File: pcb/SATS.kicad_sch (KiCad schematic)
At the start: 17 parts, among them J1 Raspberry_Pi_2_3, J2 A00-432-262-450, J3 AudioJack4_SwitchTR1, J4 1862042, J5 1862042, SW1 Main Door Switch, SW2 Serv Door Switch, SW3 Third Reed Switch, U1 MCP23017_SP, U2 MCP23017_SP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

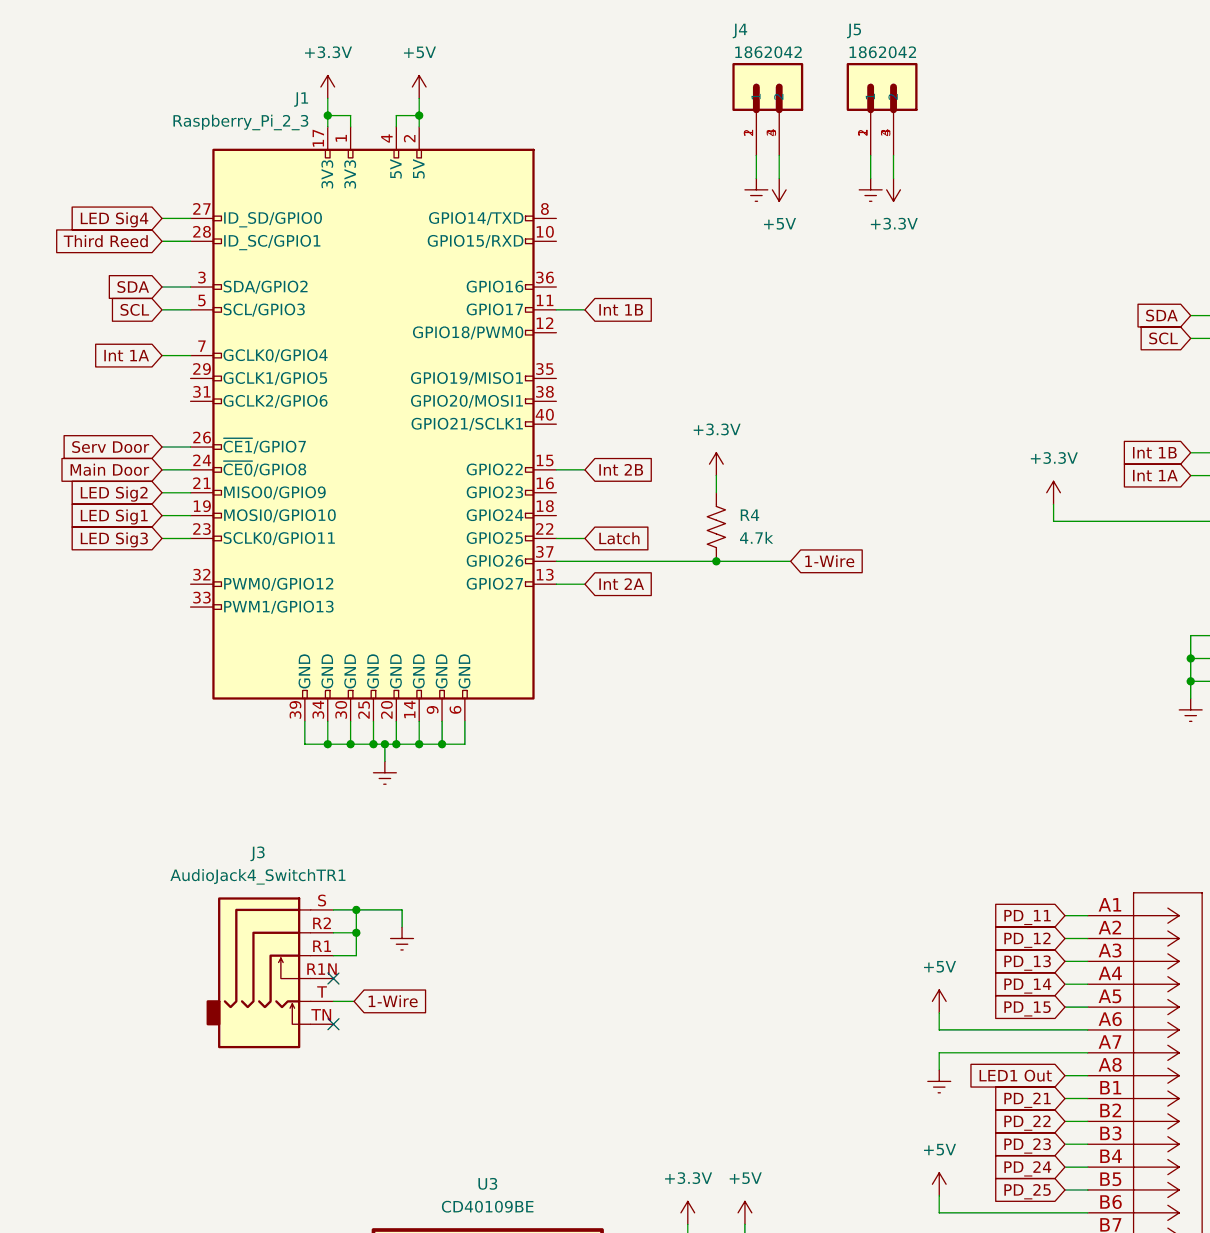
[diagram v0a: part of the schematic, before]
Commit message: Add Card LED Terminals
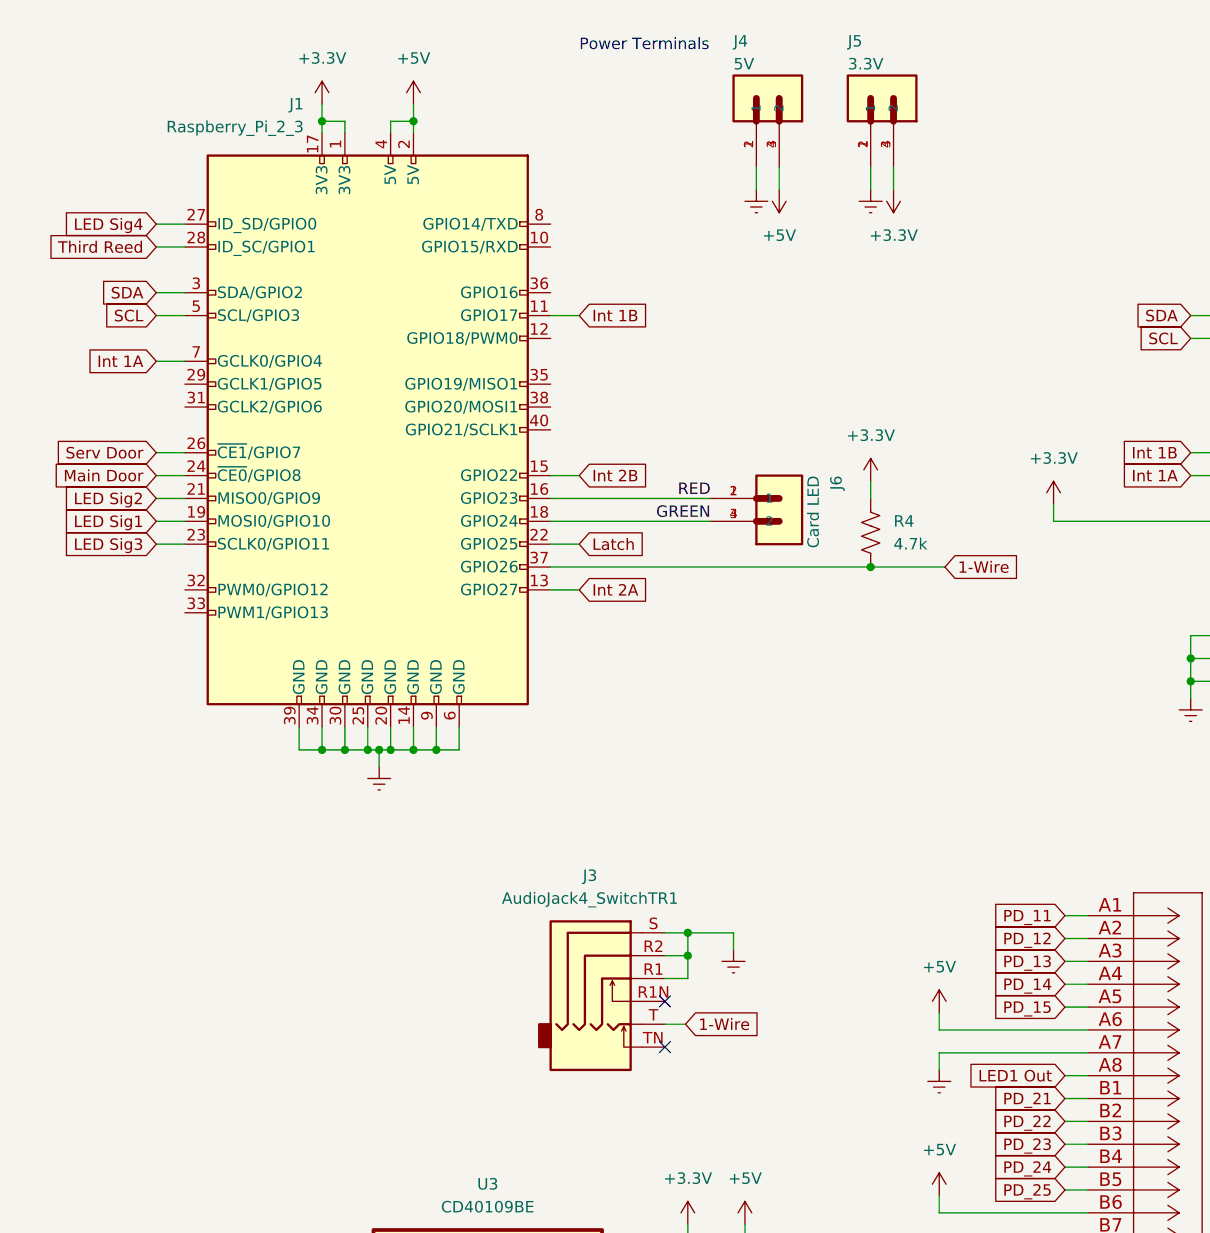
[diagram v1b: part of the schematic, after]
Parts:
- added J6: Card LED, PHOENIX_1862042, symbol TerminalConn:1862042
- J4: value 1862042 -> 5V
- J5: value 1862042 -> 3.3V
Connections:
- net RED: now reaches J1.16 (GPIO23)
- net RED: now also J6.1, J6.2 (1)
- net GREEN: now reaches J1.18 (GPIO24)
- net GREEN: now also J6.3 (2), J6.4 (2)
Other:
- note added: "Power Terminals"
- moved on the sheet: J1, J3, J4, J5, R4

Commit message: Finish Schematic
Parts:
- added C3, C4: 100nF, Capacitor_THT:C_Rect_L7.0mm_W3.5mm_P5.00mm, symbol Device:C
- added J10, J11, J12, J13: EXT_GPIO, TerminalConn:PHOENIX_1862042, symbol TerminalConn:1862042
- added J7: Wiegand, TerminalConn:PHOENIX_1862042, symbol TerminalConn:1862042
- added J8: Beep, TerminalConn:PHOENIX_1862042, symbol TerminalConn:1862042
- added J9: Card Power, TerminalConn:PHOENIX_1862042, symbol TerminalConn:1862042
- J4, J5, J6: footprint PHOENIX_1862042 -> TerminalConn:PHOENIX_1862042
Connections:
- net +3V3: now also C4.1
- net +5V: now also J4.1, J4.2 (1), C3.1, J9.1, J9.2 (1); no longer J4.3 (2), J4.4 (2)
- net Earth: now also J4.3 (2), J4.4 (2), C3.2, C4.2, J8.3 (2), J8.4 (2), J9.3 (2), J9.4 (2); no longer J4.1, J4.2 (1)
- net LED Sig1: now also U3.10 (C); no longer U3.3 (A)
- net LED Sig3: now also U3.14 (D); no longer U3.10 (C)
- net LED Sig4: now also U3.3 (A); no longer U3.14 (D)
- net LED1 Out: now also U3.11 (G); no longer U3.4 (E)
- net LED3 Out: now also U3.13 (H); no longer U3.11 (G)
- net LED4 Out: now also U3.4 (E); no longer U3.13 (H)
- net Wiegand 0: now reaches J1.10 (GPIO15/RXD)
- net Wiegand 0: now also J7.1, J7.2 (1)
- net Wiegand 1: now reaches J1.12 (GPIO18/PWM0)
- net Wiegand 1: now also J7.3 (2), J7.4 (2)
- net EXT_GPIO5: now reaches J1.29 (GCLK1/GPIO5)
- net EXT_GPIO5: now also J10.1, J10.2 (1)
- net EXT_GPIO6: now reaches J1.31 (GCLK2/GPIO6)
- net EXT_GPIO6: now also J10.3 (2), J10.4 (2)
- net EXT_GPIO12: now reaches J1.32 (PWM0/GPIO12)
- net EXT_GPIO12: now also J12.3 (2), J12.4 (2)
- net EXT_GPIO13: now reaches J1.33 (PWM1/GPIO13)
- net EXT_GPIO13: now also J11.1, J11.2 (1)
- net EXT_GPIO19: now reaches J1.35 (GPIO19/MISO1)
- net EXT_GPIO19: now also J11.3 (2), J11.4 (2)
- net EXT_GPIO16: now reaches J1.36 (GPIO16)
- net EXT_GPIO16: now also J12.1, J12.2 (1)
- net EXT_GPIO20: now reaches J1.38 (GPIO20/MOSI1)
- net EXT_GPIO20: now also J13.3 (2), J13.4 (2)
- net EXT_GPIO21: now reaches J1.40 (GPIO21/SCLK1)
- net EXT_GPIO21: now also J13.1, J13.2 (1)
- net Card Beeper: now reaches J1.8 (GPIO14/TXD)
- net Card Beeper: now also J8.1, J8.2 (1)
- net GREEN renamed Card RED
- net Card RED: now also J1.16 (GPIO23); no longer J1.18 (GPIO24)
- net RED renamed Card GRN
- net Card GRN: now also J1.18 (GPIO24); no longer J1.16 (GPIO23)
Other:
- moved on the sheet: C1, C2, D1, J1, J2, J3, J4, J5, J6, L1, R4, SW1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

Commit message: neatify and reorganize
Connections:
- net LED1 Out: now also J2.B8; no longer J2.A8
- net LED2 Out: now also J2.A8; no longer J2.B8
- net PD_11: now also J2.B1; no longer J2.A1
- net PD_12: now also J2.B2; no longer J2.A2
- net PD_13: now also J2.B3; no longer J2.A3
- net PD_14: now also J2.B4; no longer J2.A4
- net PD_15: now also J2.B5; no longer J2.A5
- net PD_21: now also J2.A1; no longer J2.B1
- net PD_22: now also J2.A2; no longer J2.B2
- net PD_23: now also J2.A3; no longer J2.B3
- net PD_24: now also J2.A4; no longer J2.B4
- net PD_25: now also J2.A5; no longer J2.B5
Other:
- moved on the sheet: C1, C2, D1, L1, R4, SW1, SW2, SW3, U1, U2, U4

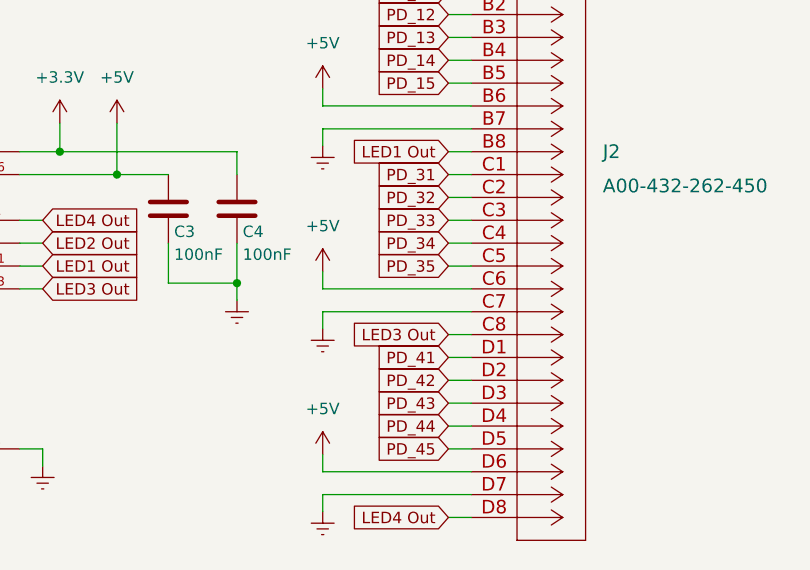
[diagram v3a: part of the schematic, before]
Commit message: Route PD lines
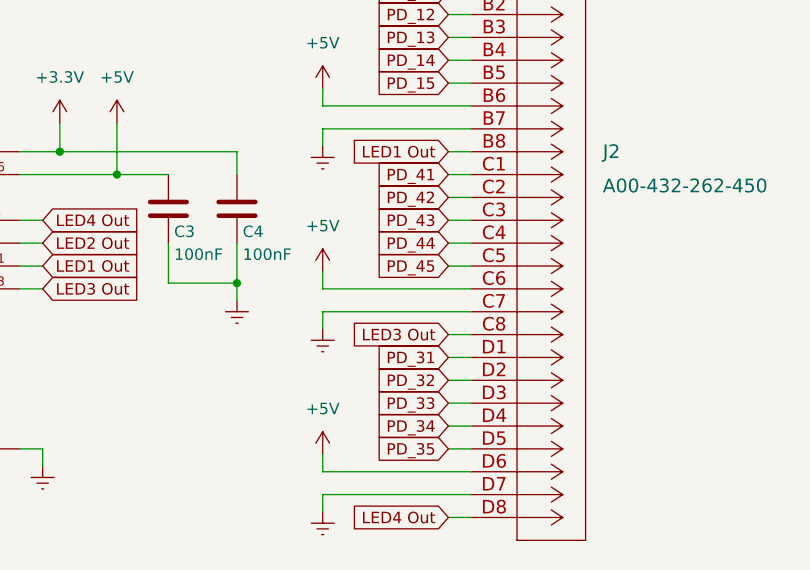
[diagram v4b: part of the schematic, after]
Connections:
- net PD_31: now also J2.D1; no longer J2.C1
- net PD_32: now also J2.D2; no longer J2.C2
- net PD_33: now also J2.D3; no longer J2.C3
- net PD_34: now also J2.D4; no longer J2.C4
- net PD_35: now also J2.D5; no longer J2.C5
- net PD_41: now also J2.C1; no longer J2.D1
- net PD_42: now also J2.C2; no longer J2.D2
- net PD_43: now also J2.C3; no longer J2.D3
- net PD_44: now also J2.C4; no longer J2.D4
- net PD_45: now also J2.C5; no longer J2.D5

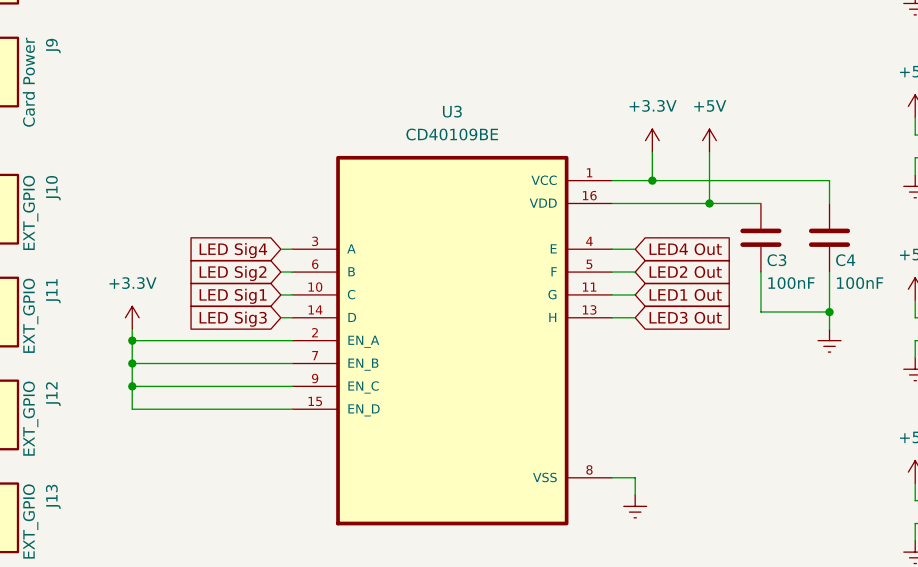
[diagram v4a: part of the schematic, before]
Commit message: Clead PD Lines and route LED Outs
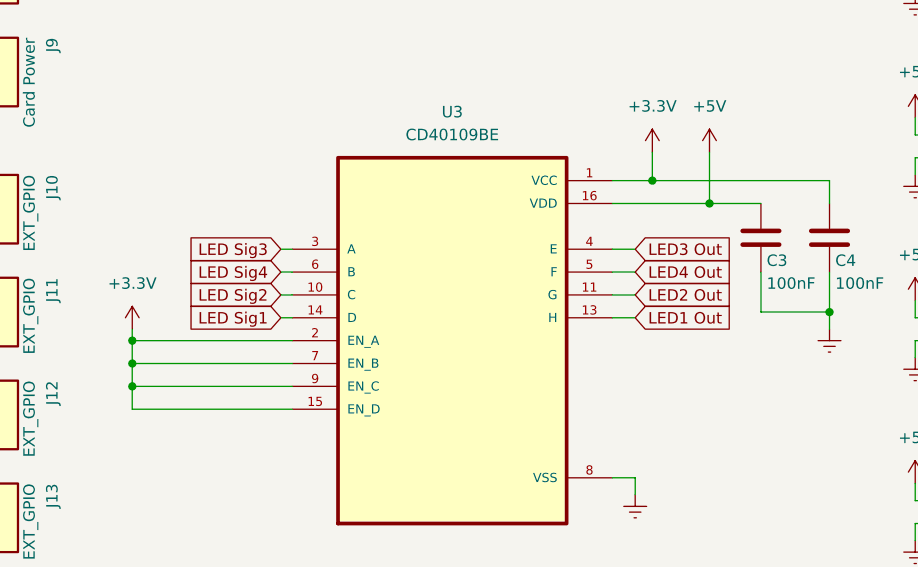
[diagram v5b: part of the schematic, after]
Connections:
- net LED Sig1: now also U3.14 (D); no longer U3.10 (C)
- net LED Sig2: now also U3.10 (C); no longer U3.6 (B)
- net LED Sig3: now also U3.3 (A); no longer U3.14 (D)
- net LED Sig4: now also U3.6 (B); no longer U3.3 (A)
- net LED1 Out: now also U3.13 (H); no longer U3.11 (G)
- net LED2 Out: now also U3.11 (G); no longer U3.5 (F)
- net LED3 Out: now also U3.4 (E); no longer U3.13 (H)
- net LED4 Out: now also U3.5 (F); no longer U3.4 (E)

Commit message: mostly done
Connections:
- net +5V: now also J9.3 (2), J9.4 (2); no longer J9.1, J9.2 (1)
- net EXT_GPIO12: now also J11.1, J11.2 (1); no longer J12.3 (2), J12.4 (2)
- net EXT_GPIO13: now also J11.3 (2), J11.4 (2); no longer J11.1, J11.2 (1)
- net EXT_GPIO19: now also J12.3 (2), J12.4 (2); no longer J11.3 (2), J11.4 (2)
- net Earth: now also J9.1, J9.2 (1); no longer J9.3 (2), J9.4 (2)
- net LED Sig1: now also J1.23 (SCLK0/GPIO11); no longer J1.19 (MOSI0/GPIO10)
- net LED Sig2: now also J1.19 (MOSI0/GPIO10); no longer J1.21 (MISO0/GPIO9)
- net LED Sig3: now also J1.27 (ID_SD/GPIO0); no longer J1.23 (SCLK0/GPIO11)
- net LED Sig4: now also J1.21 (MISO0/GPIO9); no longer J1.27 (ID_SD/GPIO0)
- net Wiegand 0: now also J7.3 (2), J7.4 (2); no longer J7.1, J7.2 (1)
- net Wiegand 1: now also J7.1, J7.2 (1); no longer J7.3 (2), J7.4 (2)
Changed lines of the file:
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@@
     (stroke (width 0) (type default) (color 0 0 0 0))
   )
-  (wire (pts (xy 20.32 138.43) (xy 34.29 138.43))
+  (wire (pts (xy 20.32 140.97) (xy 34.29 140.97))
     (stroke (width 0) (type default) (color 0 0 0 0))
   )
@@
     (stroke (width 0) (type default) (color 0 0 0 0))
   )
-  (wire (pts (xy 31.75 140.97) (xy 31.75 143.51))
+  (wire (pts (xy 31.75 138.43) (xy 31.75 143.51))
     (stroke (width 0) (type default) (color 0 0 0 0))
   )
@@
     (stroke (width 0) (type default) (color 0 0 0 0))
   )
-  (wire (pts (xy 31.75 140.97) (xy 34.29 140.97))
+  (wire (pts (xy 31.75 138.43) (xy 34.29 138.43))
     (stroke (width 0) (type default) (color 0 0 0 0))
   )
@@
     (stroke (width 0) (type default) (color 0 0 0 0))
   )
-  (wire (pts (xy 20.32 135.89) (xy 20.32 138.43))
+  (wire (pts (xy 20.32 138.43) (xy 20.32 140.97))
     (stroke (width 0) (type default) (color 0 0 0 0))
   )
@@
     )
   )
-  (global_label "LED Sig3" (shape input) (at 29.21 70.485 180) (fields_autoplaced)
+  (global_label "LED Sig3" (shape input) (at 29.21 34.925 180) (fields_autoplaced)
+    (effects (font (size 1.27 1.27)) (justify right))
+    (property "Intersheet References" "${INTERSHEET_REFS}" (id 0) (at 18.2093 35.0044 0)
+      (effects (font (size 1.27 1.27)) (justify right) hide)
+    )
+  )
+  (global_label "LED Sig1" (shape input) (at 29.21 70.485 180) (fields_autoplaced)
     (effects (font (size 1.27 1.27)) (justify right))
     (property "Intersheet References" "${INTERSHEET_REFS}" (id 0) (at 18.2093 70.4056 0)
@@
     )
   )
-  (global_label "LED Sig1" (shape input) (at 29.21 67.945 180) (fields_autoplaced)
-    (effects (font (size 1.27 1.27)) (justify right))
-    (property "Intersheet References" "${INTERSHEET_REFS}" (id 0) (at 18.2093 67.8656 0)
-      (effects (font (size 1.27 1.27)) (justify right) hide)
-    )
-  )
-  (global_label "Wiegand 0" (shape input) (at 30.48 115.57 180) (fields_autoplaced)
-    (effects (font (size 1.27 1.27)) (justify right))
-    (property "Intersheet References" "${INTERSHEET_REFS}" (id 0) (at 18.1488 115.4906 0)
+  (global_label "Wiegand 0" (shape input) (at 30.48 118.11 180) (fields_autoplaced)
+    (effects (font (size 1.27 1.27)) (justify right))
+    (property "Intersheet References" "${INTERSHEET_REFS}" (id 0) (at 18.1488 118.1894 0)
       (effects (font (size 1.27 1.27)) (justify right) hide)
     )
@@
     )
   )
-  (global_label "EXT_GPIO12" (shape input) (at 30.48 179.07 180) (fields_autoplaced)
-    (effects (font (size 1.27 1.27)) (justify right))
-    (property "Intersheet References" "${INTERSHEET_REFS}" (id 0) (at 16.8788 178.9906 0)
+  (global_label "EXT_GPIO12" (shape input) (at 30.48 165.1 180) (fields_autoplaced)
+    (effects (font (size 1.27 1.27)) (justify right))
+    (property "Intersheet References" "${INTERSHEET_REFS}" (id 0) (at 16.8788 165.0206 0)
       (effects (font (size 1.27 1.27)) (justify right) hide)
     )
@@
     )
   )
-  (global_label "EXT_GPIO13" (shape input) (at 30.48 165.1 180) (fields_autoplaced)
-    (effects (font (size 1.27 1.27)) (justify right))
-    (property "Intersheet References" "${INTERSHEET_REFS}" (id 0) (at 16.8788 165.0206 0)
+  (global_label "EXT_GPIO13" (shape input) (at 30.48 167.64 180) (fields_autoplaced)
+    (effects (font (size 1.27 1.27)) (justify right))
+    (property "Intersheet References" "${INTERSHEET_REFS}" (id 0) (at 16.8788 167.7194 0)
       (effects (font (size 1.27 1.27)) (justify right) hide)
     )
@@
     )
   )
-  (global_label "EXT_GPIO19" (shape input) (at 30.48 167.64 180) (fields_autoplaced)
-    (effects (font (size 1.27 1.27)) (justify right))
-    (property "Intersheet References" "${INTERSHEET_REFS}" (id 0) (at 16.8788 167.5606 0)
+  (global_label "EXT_GPIO19" (shape input) (at 30.48 179.07 180) (fields_autoplaced)
+    (effects (font (size 1.27 1.27)) (justify right))
+    (property "Intersheet References" "${INTERSHEET_REFS}" (id 0) (at 16.8788 179.1494 0)
       (effects (font (size 1.27 1.27)) (justify right) hide)
     )
@@
     )
   )
-  (global_label "Wiegand 1" (shape input) (at 30.48 118.11 180) (fields_autoplaced)
-    (effects (font (size 1.27 1.27)) (justify right))
-    (property "Intersheet References" "${INTERSHEET_REFS}" (id 0) (at 18.1488 118.0306 0)
+  (global_label "Wiegand 1" (shape input) (at 30.48 115.57 180) (fields_autoplaced)
+    (effects (font (size 1.27 1.27)) (justify right))
+    (property "Intersheet References" "${INTERSHEET_REFS}" (id 0) (at 18.1488 115.6494 0)
       (effects (font (size 1.27 1.27)) (justify right) hide)
     )
@@
     )
   )
-  (global_label "LED Sig4" (shape input) (at 29.21 34.925 180) (fields_autoplaced)
-    (effects (font (size 1.27 1.27)) (justify right))
-    (property "Intersheet References" "${INTERSHEET_REFS}" (id 0) (at 18.2093 34.8456 0)
+  (global_label "LED Sig4" (shape input) (at 29.21 65.405 180) (fields_autoplaced)
+    (effects (font (size 1.27 1.27)) (justify right))
+    (property "Intersheet References" "${INTERSHEET_REFS}" (id 0) (at 18.2093 65.3256 0)
       (effects (font (size 1.27 1.27)) (justify right) hide)
     )
@@
     )
   )
-  (global_label "LED Sig2" (shape input) (at 29.21 65.405 180) (fields_autoplaced)
-    (effects (font (size 1.27 1.27)) (justify right))
-    (property "Intersheet References" "${INTERSHEET_REFS}" (id 0) (at 18.2093 65.3256 0)
+  (global_label "LED Sig2" (shape input) (at 29.21 67.945 180) (fields_autoplaced)
+    (effects (font (size 1.27 1.27)) (justify right))
+    (property "Intersheet References" "${INTERSHEET_REFS}" (id 0) (at 18.2093 68.0244 0)
       (effects (font (size 1.27 1.27)) (justify right) hide)
     )
@@
     (pin "1")
   )
-  (symbol (lib_id "power:+5V") (at 20.32 135.89 0) (mirror y) (unit 1)
-    (in_bom yes) (on_board yes) (fields_autoplaced)
-    (property "Reference" "#PWR0135" (id 0) (at 20.32 139.7 0)
-      (effects (font (size 1.27 1.27)) hide)
-    )
-    (property "Value" "+5V" (id 1) (at 22.86 134.6199 0)
-      (effects (font (size 1.27 1.27)) (justify right))
-    )
-    (property "Footprint" "" (id 2) (at 20.32 135.89 0)
-      (effects (font (size 1.27 1.27)) hide)
-    )
-    (property "Datasheet" "" (id 3) (at 20.32 135.89 0)
-      (effects (font (size 1.27 1.27)) hide)
-    )
+  (symbol (lib_id "power:+5V") (at 20.32 138.43 0) (mirror y) (unit 1)
+    (in_bom yes) (on_board yes) (fields_autoplaced)
+    (property "Reference" "#PWR0135" (id 0) (at 20.32 142.24 0)
+      (effects (font (size 1.27 1.27)) hide)
+    )
+    (property "Value" "+5V" (id 1) (at 22.86 137.1599 0)
+      (effects (font (size 1.27 1.27)) (justify right))
+    )
+    (property "Footprint" "" (id 2) (at 20.32 138.43 0)
+      (effects (font (size 1.27 1.27)) hide)
+    )
+    (property "Datasheet" "" (id 3) (at 20.32 138.43 0)
+      (effects (font (size 1.27 1.27)) hide)
+    )
